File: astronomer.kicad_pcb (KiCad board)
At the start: 2 copper layers, 46 parts, among them J1 6P6C, SW1 SW_Push_45deg, SW10 SW_Push_45deg, SW11 SW_Push_45deg, SW12 SW_Push_45deg, SW13 SW_Push_45deg, SW14 SW_Push_45deg, SW15 SW_Push_45deg, SW16 SW_Push_45deg, SW17 SW_Push_45deg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

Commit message: traces
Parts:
- moved D9 18.9 mm to (209.6, 67.1)
- moved SW3 18.9 mm to (200.1, 47.0)
- moved U1 18.9 mm to (143.1, 43.2)
- moved D1 18.9 mm to (171.6, 57.8)
- moved D10 18.9 mm to (228.6, 71.0)
- moved D11 18.9 mm to (247.6, 77.2)
- moved D12 18.9 mm to (267.8, 80.9)
- moved D13 18.9 mm to (171.6, 94.4)
- moved D14 18.9 mm to (190.6, 91.6)
- moved D15 18.9 mm to (209.6, 86.8)
- moved D16 18.9 mm to (228.6, 89.6)
- moved D17 18.9 mm to (247.6, 95.5)
- moved D18 18.9 mm to (267.8, 99.7)
- moved D19 18.9 mm to (151.5, 94.9)
- moved D2 18.9 mm to (190.6, 54.2)
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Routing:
- net /Row 3: track 0.00 -> 153.6 mm, vias 0 -> 5
- net /Row 2: track 0.00 -> 146.4 mm, vias 0 -> 11
- net /Row 1: track 0.42 -> 146.6 mm, vias 0 -> 11
- net /Row 4: track 0.00 -> 98.7 mm, vias 0 -> 3
- net Net-(D16-A): track 0.00 -> 6.18 mm
- net Net-(D18-A): track 0.00 -> 5.59 mm
- net Net-(D17-A): track 0.00 -> 5.38 mm

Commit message: pcb lights
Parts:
- added C1: C_Small, Capacitor_SMD:C_1206_3216Metric, B.Cu at (154.8, 52.1)
- added C2: C_Small, Capacitor_SMD:C_1206_3216Metric, F.Cu at (75.8, 65.2)
- added C3: C_Small, Capacitor_SMD:C_1206_3216Metric, F.Cu at (75.8, 68.6)
- added C4: C_Small, Capacitor_SMD:C_1206_3216Metric, F.Cu at (75.8, 71.9)
- added C5: C_Small, Capacitor_SMD:C_1206_3216Metric, F.Cu at (75.8, 75.3)
- added C6: C_Small, Capacitor_SMD:C_1206_3216Metric, F.Cu at (75.8, 78.6)
- added C7: C_Small, Capacitor_SMD:C_1206_3216Metric, F.Cu at (75.8, 82.0)
- added C8: C_Small, Capacitor_SMD:C_1206_3216Metric, F.Cu at (75.8, 85.3)
- added D23: SK6812MINI, Keyboard:SK6812-MINI-E, B.Cu at (165.8, 51.3)
- added D24: SK6812MINI, Keyboard:SK6812-MINI-E, B.Cu at (184.8, 46.8)
- added D25: SK6812MINI, Keyboard:SK6812-MINI-E, B.Cu at (203.8, 41.5)
- added D26: SK6812MINI, Keyboard:SK6812-MINI-E, B.Cu at (222.5, 44.5)
- added D27: SK6812MINI, Keyboard:SK6812-MINI-E, B.Cu at (241.5, 51.3)
- added D28: SK6812MINI, Keyboard:SK6812-MINI-E, B.Cu at (260.8, 55.8)
- added D29: SK6812MINI, Keyboard:SK6812-MINI-E, B.Cu at (165.8, 69.3)
- added D30: SK6812MINI, Keyboard:SK6812-MINI-E, B.Cu at (184.8, 64.8)
- added D31: SK6812MINI, Keyboard:SK6812-MINI-E, B.Cu at (203.8, 59.5)
- added D32: SK6812MINI, Keyboard:SK6812-MINI-E, B.Cu at (222.5, 62.5)
- added D33: SK6812MINI, Keyboard:SK6812-MINI-E, B.Cu at (241.8, 69.3)
- added D34: SK6812MINI, Keyboard:SK6812-MINI-E, B.Cu at (260.8, 73.8)
- added D35: SK6812MINI, Keyboard:SK6812-MINI-E, B.Cu at (165.8, 87.3)
- added D36: SK6812MINI, Keyboard:SK6812-MINI-E, B.Cu at (184.8, 82.8)
- added D37: SK6812MINI, Keyboard:SK6812-MINI-E, B.Cu at (203.8, 77.7)
- added D38: SK6812MINI, Keyboard:SK6812-MINI-E, B.Cu at (222.8, 80.5)
- added D39: SK6812MINI, Keyboard:SK6812-MINI-E, B.Cu at (241.7, 87.3)
- added D40: SK6812MINI, Keyboard:SK6812-MINI-E, B.Cu at (260.8, 91.8)
- added D41: SK6812MINI, Keyboard:SK6812-MINI-E, B.Cu at (136.7, 94.0)
- added D42: SK6812MINI, Keyboard:SK6812-MINI-E, B.Cu at (140.8, 112.6)
- added D43: SK6812MINI, Keyboard:SK6812-MINI-E, B.Cu at (163.1, 107.0)
- added D44: SK6812MINI, Keyboard:SK6812-MINI-E, B.Cu at (188.0, 107.3)
- moved D19 25.1 mm to (131.0, 109.5)
- moved D22 21.8 mm to (176.4, 119.1)
- moved D21 20.9 mm to (156.8, 122.7)
- moved D20 20.7 mm to (139.0, 129.2)
- moved D12 17.9 mm to (251.2, 87.6)
- moved D6 17.9 mm to (251.2, 69.6)
- moved D18 17.6 mm to (251.2, 105.6)
- moved D7 17.0 mm to (156.5, 84.2)
- moved D1 16.9 mm to (156.5, 65.4)
- moved D11 16.7 mm to (232.2, 83.6)
- moved D9 16.6 mm to (194.2, 73.2)
- moved D17 16.6 mm to (232.2, 101.6)
- moved D3 16.6 mm to (194.2, 55.0)
- moved D4 16.6 mm to (213.2, 58.3)
- moved D5 16.6 mm to (232.2, 64.8)
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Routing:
- net /Col 6: track 180.0 -> 0.00 mm
- net /Col 4: track 172.8 -> 0.00 mm
- net /Col 3: track 159.8 -> 0.00 mm
- net /Col 5: track 156.3 -> 0.00 mm
- net /Row 3: track 153.6 -> 0.00 mm, vias 5 -> 0
- net /Row 1: track 146.6 -> 0.00 mm, vias 11 -> 0
- net /Row 2: track 146.4 -> 0.00 mm, vias 11 -> 0
- net /Col 2: track 137.2 -> 0.00 mm
- net /Row 4: track 98.7 -> 0.00 mm, vias 3 -> 0
- net /Col 1: track 76.7 -> 0.00 mm
- net Net-(D19-A): track 7.34 -> 0.00 mm
- net Net-(D20-A): track 6.97 -> 0.00 mm
- net Net-(D15-A): track 6.36 -> 0.00 mm
- net Net-(D16-A): track 6.18 -> 0.00 mm
- net Net-(D14-A): track 5.94 -> 0.00 mm
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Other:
- board outline added: 225.3 x 98.7 mm

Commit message: caps
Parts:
- C2, C3, C4, C5, C6, C7, C8: moved to B.Cu
- moved C2 138.4 mm to (213.0, 47.1), turned to -90 degrees
- moved C4 137.6 mm to (213.2, 64.8), turned to 90 degrees
- moved C6 137.5 mm to (213.2, 82.9), turned to -90 degrees
- moved C7 125.5 mm to (199.0, 105.9), turned to -90 degrees
- moved D29 95.4 mm to (261.0, 73.8), turned to 0 degrees
- moved D34 95.4 mm to (165.5, 69.3), turned to 0 degrees
- moved C8 80.6 mm to (152.4, 110.4), turned to -90 degrees
- moved C5 79.4 mm to (153.9, 89.5), turned to -90 degrees
- moved C3 79.0 mm to (154.8, 71.6), turned to 90 degrees
- moved D33 57.5 mm to (184.5, 64.8), turned to 0 degrees
- moved D30 56.9 mm to (241.5, 69.3), turned to 0 degrees
- moved D44 53.0 mm to (136.7, 93.9), turned to 30 degrees
- moved D41 53.0 mm to (188.0, 107.3), turned to -10 degrees
- moved D42 23.0 mm to (163.1, 107.0), turned to 12 degrees
- moved D43 22.6 mm to (141.1, 112.3), turned to 30 degrees
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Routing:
- net Net-(D40-DOUT): track 0.00 -> 84.4 mm
- net Net-(D28-DOUT): track 0.00 -> 23.2 mm
- net Net-(D43-DOUT): track 0.00 -> 23.0 mm
- net Net-(D41-DOUT): track 0.00 -> 20.4 mm
- net Net-(D42-DOUT): track 0.00 -> 19.3 mm
- net Net-(D34-DOUT): track 0.00 -> 19.3 mm
- net Net-(D24-DOUT): track 0.00 -> 17.1 mm
- net Net-(D36-DOUT): track 0.00 -> 16.9 mm
- net Net-(D23-DOUT): track 0.00 -> 16.8 mm
- net Net-(D32-DOUT): track 0.00 -> 16.7 mm
- net Net-(D35-DOUT): track 0.00 -> 16.7 mm
- net Net-(D33-DOUT): track 0.00 -> 16.1 mm
- net Net-(D26-DOUT): track 0.00 -> 15.8 mm
- net Net-(D38-DOUT): track 0.00 -> 15.8 mm
- net Net-(D30-DOUT): track 0.00 -> 15.5 mm
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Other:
- board size 225.3 x 98.7 mm -> 4.6 x 4.4 mm

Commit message: more traces
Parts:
- moved D2 1.97 mm to (175.1, 60.0)
- moved D19 1.15 mm to (131.3, 110.6)
- moved D8 1.13 mm to (175.1, 78.6)
- moved D12 0.23 mm to (251.1, 87.4)
- moved D14 0.15 mm to (175.1, 96.6)
- moved D9 0.15 mm to (194.1, 73.2)
- moved D3 0.15 mm to (194.1, 55.0)
- moved D10 0.15 mm to (213.1, 76.3)
- moved D4 0.15 mm to (213.1, 58.3)
- moved D5 0.14 mm to (232.1, 64.8)
- moved D6 0.14 mm to (251.1, 69.6)
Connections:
- D23 pad 3: unconnected-(D23-DIN-Pad3) -> /LED
- J1 pad 2: /LED -> /LED_TXRX
- U1 pad 8: unconnected-(U1-GP8-Pad8) -> /LED
- U1 pad 9: unconnected-(U1-GP9-Pad9) -> /LED_TXRX
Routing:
- net /Col 4: track 0.00 -> 177.5 mm, vias 0 -> 7
- net /Col 6: track 0.00 -> 171.0 mm, vias 0 -> 3
- net /Col 3: track 0.00 -> 152.0 mm, vias 0 -> 7
- net /Row 3: track 0.00 -> 146.5 mm, vias 0 -> 2
- net /Col 5: track 0.00 -> 141.4 mm, vias 0 -> 5
- net /Row 2: track 0.00 -> 134.8 mm, vias 0 -> 4
- net /Col 2: track 0.00 -> 128.2 mm, vias 0 -> 6
- net /Row 1: track 0.00 -> 126.9 mm
- net /Row 4: track 0.00 -> 107.7 mm
- net /Col 1: track 0.00 -> 82.0 mm, vias 0 -> 4
- net /LED: track 0.00 -> 53.4 mm, vias 0 -> 1
- net /RX: track 0.00 -> 39.4 mm
- net /TX: track 0.00 -> 38.5 mm
- net /LED_TXRX: track 0.00 -> 11.3 mm
- net Net-(D8-A): track 0.00 -> 4.80 mm
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
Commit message: more traces
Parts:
- moved D34 0.89 mm to (164.6, 69.3)
- moved D33 0.74 mm to (183.7, 64.8)
- moved D36 0.73 mm to (184.2, 82.4)
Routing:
- net GND: track 0.00 -> 297.3 mm, vias 0 -> 3
- net /Row 3: track 146.5 -> 113.8 mm
- net +5V: track 0.00 -> 24.7 mm
- net /Col 4: track 177.5 -> 174.5 mm
- net /Row 2: track 134.8 -> 136.3 mm, vias 4 -> 6
- net Net-(D33-DOUT): track 16.1 -> 17.0 mm
- net /Row 4: track 107.7 -> 108.5 mm
- net Net-(D35-DOUT): track 16.7 -> 15.8 mm
- net Net-(D42-DOUT): track 19.3 -> 18.7 mm, vias 0 -> 2
- added copper zone on B.Cu, net +5V
- added copper zone on F.Cu, net GND
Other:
- board size 4.6 x 4.4 mm -> 157.1 x 100 mm

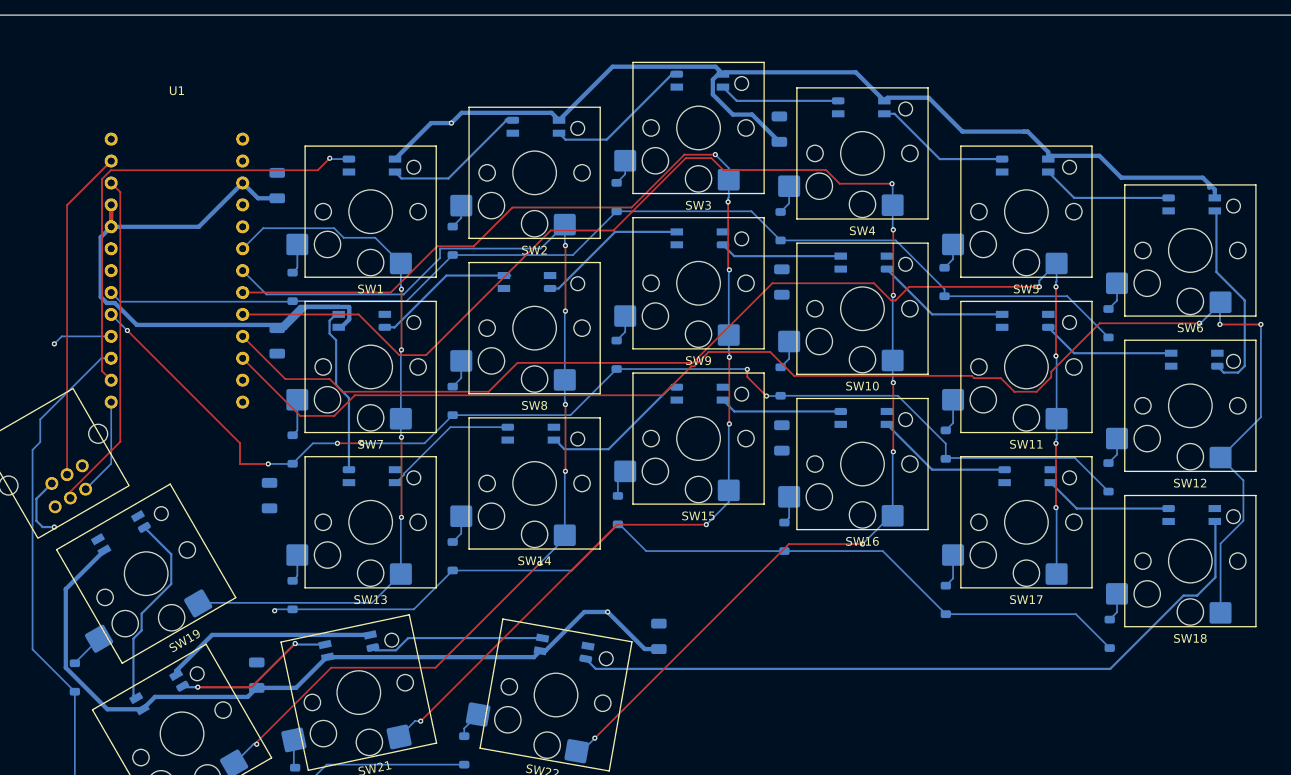
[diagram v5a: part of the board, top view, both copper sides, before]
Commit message: fixed footprints
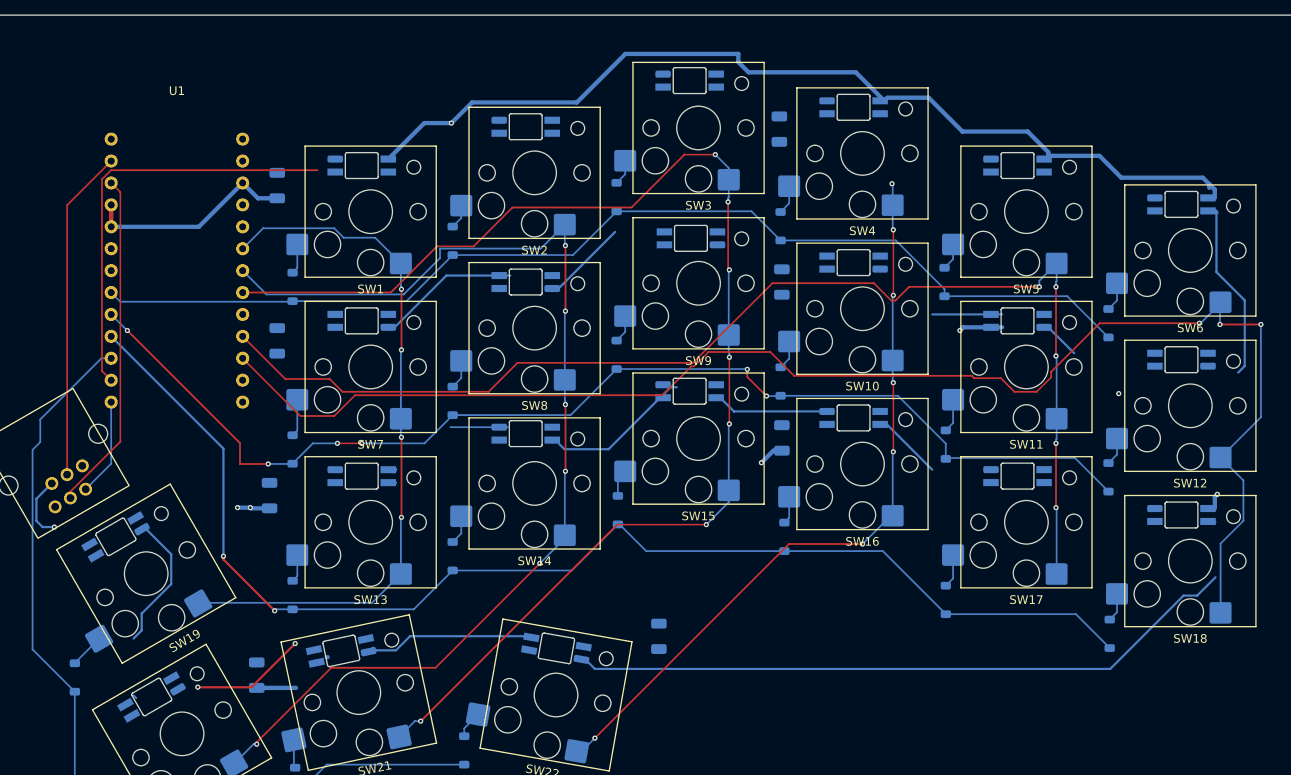
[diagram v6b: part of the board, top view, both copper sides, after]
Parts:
- moved D29 1.48 mm to (259.6, 73.8)
- moved D37 1.22 mm to (202.6, 77.5)
- moved D25 1.19 mm to (202.6, 41.5)
- moved D23 1.19 mm to (164.6, 51.3)
- moved D24 1.19 mm to (183.6, 46.8)
- moved D28 1.19 mm to (259.6, 55.8)
- moved D35 1.19 mm to (164.6, 87.3)
- moved D38 1.19 mm to (221.6, 80.5)
- moved D40 1.19 mm to (259.6, 91.8)
- moved D39 1.18 mm to (240.6, 87.3)
- moved D31 1.18 mm to (221.6, 62.5)
- moved D42 1.05 mm to (162.2, 107.5)
- moved D43 1.05 mm to (140.2, 112.9)
- moved D32 1.04 mm to (202.7, 59.7)
- moved D41 0.89 mm to (187.1, 107.3)
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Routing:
- net GND: track 297.3 -> 160.9 mm, vias 3 -> 8
- net /Col 4: track 174.5 -> 86.6 mm
- net /Row 3: track 113.8 -> 146.5 mm
- net +5V: track 24.7 -> 0.00 mm
- net Net-(D34-DOUT): track 19.6 -> 0.00 mm
- net Net-(D24-DOUT): track 17.1 -> 0.00 mm
- net Net-(D23-DOUT): track 16.8 -> 0.00 mm
- net Net-(D26-DOUT): track 15.8 -> 0.00 mm
- net Net-(D27-DOUT): track 15.2 -> 0.00 mm
- net Net-(D39-DOUT): track 14.9 -> 0.00 mm
- net Net-(D31-DOUT): track 14.2 -> 0.00 mm
- net Net-(D25-DOUT): track 14.0 -> 0.00 mm
- net Net-(D29-DOUT): track 15.5 -> 4.24 mm
- net Net-(D35-DOUT): track 15.8 -> 7.09 mm
- net Net-(D38-DOUT): track 15.8 -> 7.91 mm
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
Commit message: revisions
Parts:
- moved D22 51.1 mm to (126.0, 111.0), turned to -90 degrees
- moved D21 29.2 mm to (130.1, 111.0), turned to -90 degrees
- moved D20 27.9 mm to (126.1, 104.5), turned to -90 degrees
- moved C3 16.3 mm to (170.1, 66.1), turned to 0 degrees
- moved C4 15.0 mm to (227.2, 59.3), turned to 0 degrees
- moved C8 12.4 mm to (162.9, 103.9), turned to -168 degrees
- moved C7 8.37 mm to (191.0, 103.5), turned to 80 degrees
- moved D19 6.26 mm to (130.1, 104.5), turned to -90 degrees
- moved C5 4.02 mm to (157.9, 89.3), turned to 180 degrees
- moved C1 3.18 mm to (157.6, 52.1), turned to 180 degrees
- moved C2 2.45 mm to (214.6, 45.2), turned to 180 degrees
- moved C6 1.90 mm to (214.6, 81.5), turned to 180 degrees
- moved D7 0.99 mm to (156.5, 83.2)
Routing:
- net GND: track 160.9 -> 0.00 mm, vias 8 -> 0
- net Net-(D40-DOUT): track 78.0 -> 0.00 mm
- net /Row 4: track 108.5 -> 47.0 mm
- net Net-(D22-A): track 3.17 -> 60.8 mm
- net /LED: track 49.2 -> 0.00 mm
- net Net-(D21-A): track 3.28 -> 30.5 mm
- net /Col 6: track 171.0 -> 196.4 mm, vias 3 -> 2
- net Net-(D20-A): track 3.20 -> 25.4 mm
- net Net-(D28-DOUT): track 20.5 -> 0.00 mm
- net Net-(D41-DOUT): track 20.1 -> 0.00 mm
- net Net-(D33-DOUT): track 17.0 -> 0.00 mm
- net Net-(D36-DOUT): track 16.9 -> 0.00 mm
- net Net-(D43-DOUT): track 16.4 -> 0.21 mm
- net Net-(D42-DOUT): track 13.7 -> 0.00 mm, vias 2 -> 0
- net Net-(D37-DOUT): track 13.0 -> 0.00 mm
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- removed copper zone on B.Cu, net +5V

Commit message: revisions
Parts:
- moved C8 1.46 mm to (161.6, 103.2)
- moved C4 1.05 mm to (226.3, 59.9)
- moved C3 0.15 mm to (170.2, 66.1)
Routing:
- net +5V: track 0.00 -> 746.0 mm, vias 0 -> 24
- net Net-(D40-DOUT): track 0.00 -> 97.9 mm, vias 0 -> 2
- net /Col 4: track 93.5 -> 176.4 mm, vias 6 -> 8
- net GND: track 0.00 -> 56.1 mm, vias 0 -> 33
- net /LED: track 0.00 -> 45.2 mm, vias 0 -> 2
- net Net-(D28-DOUT): track 0.00 -> 26.2 mm, vias 0 -> 2
- net Net-(D43-DOUT): track 0.21 -> 24.1 mm
- net Net-(D34-DOUT): track 0.00 -> 20.5 mm, vias 0 -> 2
- net Net-(D41-DOUT): track 0.00 -> 19.6 mm, vias 0 -> 2
- net Net-(D42-DOUT): track 0.00 -> 17.7 mm, vias 0 -> 2
- net Net-(D32-DOUT): track 0.00 -> 17.2 mm, vias 0 -> 2
- net Net-(D36-DOUT): track 0.00 -> 16.7 mm
- net Net-(D24-DOUT): track 0.00 -> 16.2 mm, vias 0 -> 2
- net Net-(D33-DOUT): track 0.00 -> 16.1 mm, vias 0 -> 2
- net Net-(D35-DOUT): track 0.00 -> 16.0 mm
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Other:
- board size 157.1 x 100 mm -> 151.7 x 94.8 mm
